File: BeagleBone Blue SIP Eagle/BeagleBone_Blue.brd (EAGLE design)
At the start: 86.4 x 54.6 mm, 281 parts, among them M1 JST_ZH_2, M2 JST_ZH_2, M3 JST_ZH_2, M4 JST_ZH_2, P10 SCHA5B0200, Q3 MOSFET-N, U1 TPD4S012_DRY_6, U4 TPD4S012_DRY_6, U5 24LC_32AT-I/OT, U6 SN74LVC1G07_DCK_5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

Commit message: swap to MicroUSB connector
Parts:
- removed OTG: UX60SC-MB-5ST(80), BeagleBone_Blue:UX60SC-MB-5ST(80)
- added JP1: (no value), Strawson_Eagle_Lib:USB-AB-MICRO-SMD
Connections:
- net GND: now also JP1.GND, JP1.SHIELD1, JP1.SHIELD2, JP1.SHIELD3, JP1.SHIELD4; no longer OTG.5, OTG.M1, OTG.M2, OTG.M3, OTG.M4
- net N$117: now also JP1.D+; no longer OTG.3
- net N$118: now also JP1.D-; no longer OTG.2
- net N$119: now also JP1.ID; no longer OTG.4
- net USB0_VBUS: now also JP1.VBUS; no longer OTG.1

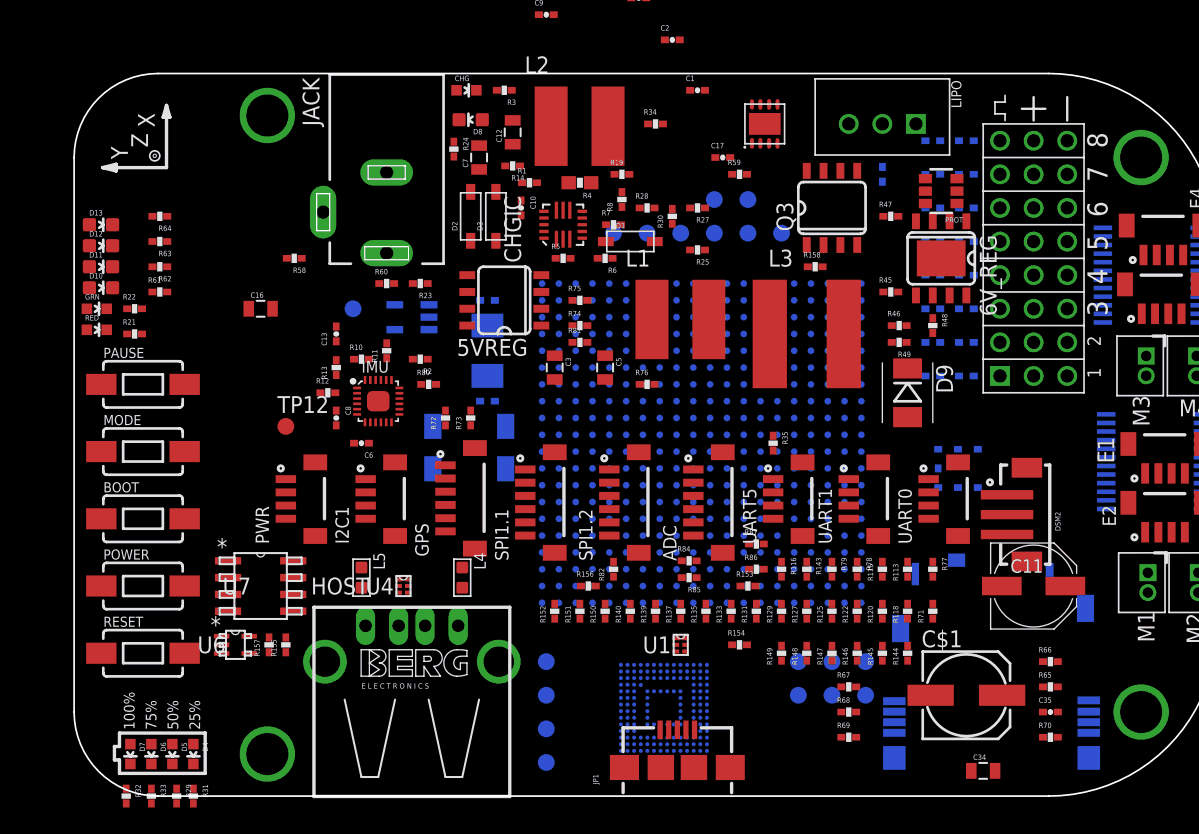
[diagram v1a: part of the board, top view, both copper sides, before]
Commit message: shuffle left side of board and tweak silkscreen for EEPROM
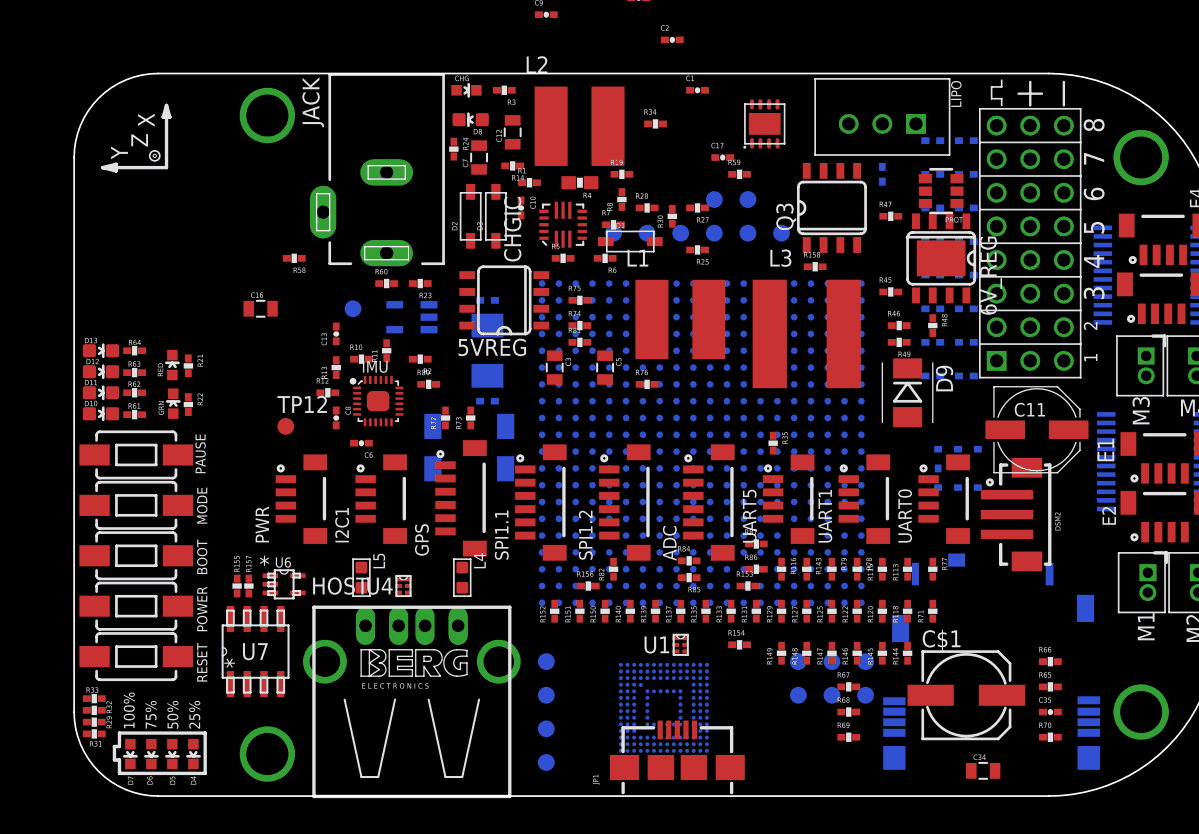
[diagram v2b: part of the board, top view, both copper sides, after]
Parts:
- moved C11 11.8 mm to (72.8, -26.9)
- moved R64 10.3 mm to (4.57, -21.0), turned to 0 degrees
- moved R63 10.1 mm to (4.57, -22.6)
- moved R62 9.71 mm to (4.57, -24.1)
- moved D10 9.53 mm to (2.03, -25.7)
- moved D12 9.53 mm to (2.03, -22.5)
- moved D11 9.52 mm to (2.03, -24.1)
- moved D13 9.52 mm to (2.03, -21.0)
- moved R61 9.46 mm to (4.57, -25.8)
- moved GRN 9.21 mm to (7.49, -25.0), turned to 0 degrees
- moved R31 8.84 mm to (1.52, -49.9), turned to 0 degrees
- moved R33 8.54 mm to (1.52, -47.2), turned to 0 degrees
- moved R29 8.36 mm to (1.52, -49.0), turned to 0 degrees
- moved R22 8.30 mm to (8.64, -25.0), turned to 270 degrees
- moved R32 6.91 mm to (1.52, -48.1), turned to 0 degrees
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
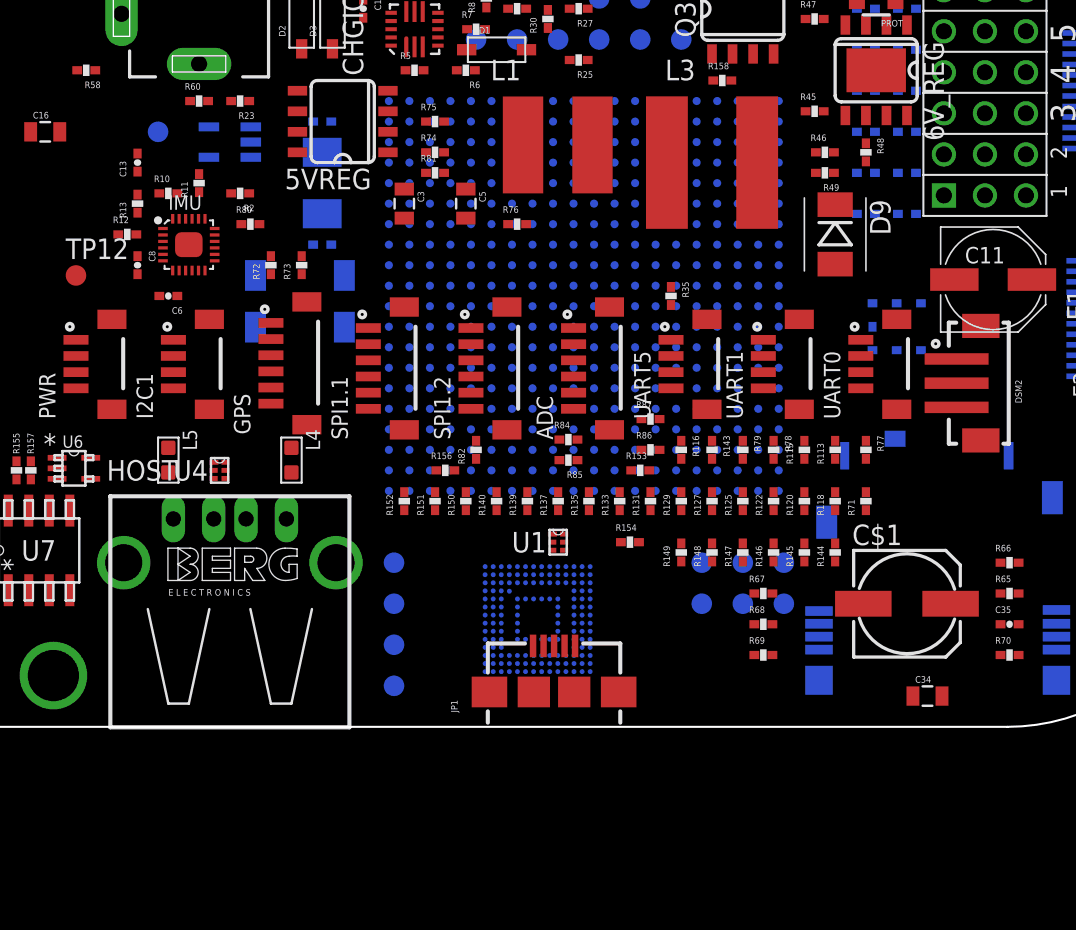
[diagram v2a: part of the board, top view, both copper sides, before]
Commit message: fix incorrect name and origin for usb host port and capacitor in library
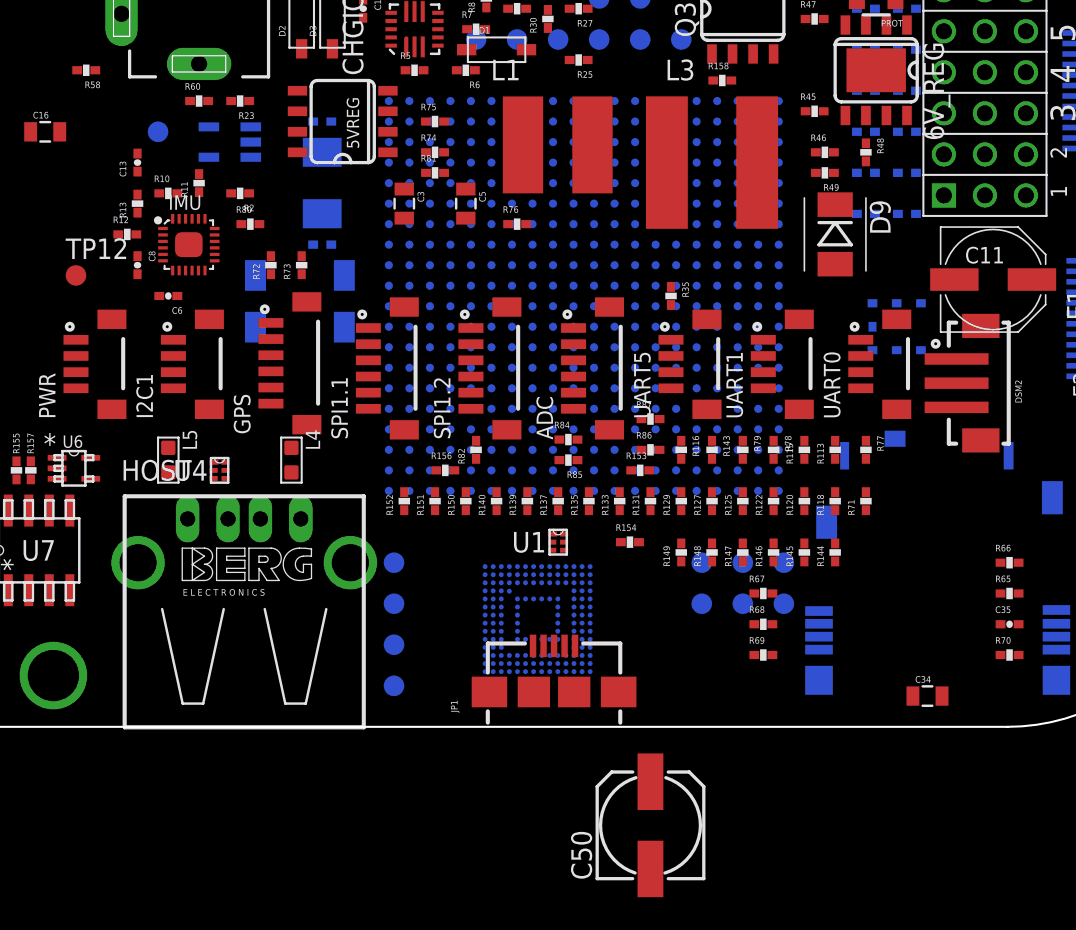
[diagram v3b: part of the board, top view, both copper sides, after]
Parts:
- removed C$1: AVE107M06D16T-F, BeagleBone_Blue:AVE107M06D16T-F
- added C50: AVE107M06D16T-F, BeagleBone_Blue:AVE107M06D16T-F
- moved HOST 10.6 mm to (26.4, -48.0)
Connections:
- net GND: now also C50.-; no longer C$1.-
- net N$127: now also C50.+; no longer C$1.+
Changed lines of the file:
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@@
 <attribute name="VALUE" x="1.699" y="-39.149" size="0.762" layer="27"/>
 </element>
-<element name="C$1" library="BeagleBone_Blue" package="AVE107M06D16T-F" value="AVE107M06D16T-F" x="80.137" y="-49.53"/>
+<element name="C50" library="BeagleBone_Blue" package="AVE107M06D16T-F" value="AVE107M06D16T-F" x="51.562" y="-60.706" rot="R90"/>
 <element name="C1" library="Strawson_Eagle_Lib" package="0402-CAP" value="0.1uF" x="47.117" y="-1.27"/>
 <element name="C10" library="Strawson_Eagle_Lib" package="0402-CAP" value="1uF" x="33.782" y="-10.16" rot="R270"/>
@@
 <element name="H1" library="SparkFun" package="SSOP24" value="TB6621FNG" x="81.407" y="-15.24" rot="MR270"/>
 <element name="H2" library="SparkFun" package="SSOP24" value="TB6621FNG" x="81.661" y="-29.337" rot="MR270"/>
-<element name="HOST" library="BeagleBone_Blue" package="87520-0010BLF" value="87520-0010BLF" x="36.957" y="-46.99"/>
+<element name="HOST" library="BeagleBone_Blue" package="87520-0010BLF" value="87520-0010BLF" x="26.416" y="-48.006"/>
 <element name="I2C1" library="Strawson_Eagle_Lib" package="JST_SH_4_SMD" value="JST_SH_4" x="23.3045" y="-31.115" rot="R90"/>
 <element name="IMU" library="Strawson_Eagle_Lib" package="QFN24G-0.4-3X3MM" value="MPU-9250" x="22.987" y="-24.765">
@@
 <element name="E$1" library="Strawson_Eagle_Lib" package="BATTERY_INDICATOR" value="" x="6.731" y="-51.3715"/>
 <element name="BOARD" library="Strawson_Eagle_Lib" package="BEAGLEBONE_BLUE_NO_HOLES" value="" x="0" y="0" rot="R270"/>
-<element name="5VREG" library="BeagleBone_Blue" package="SO08-TIGHT" value="AP1509SOIC-8-TIGHT" x="32.512" y="-17.145" rot="R90"/>
+<element name="5VREG" library="BeagleBone_Blue" package="SO08-TIGHT" value="AP1509SOIC-8-TIGHT" x="32.512" y="-17.145" smashed="yes" rot="R90">
+<attribute name="VALUE" x="33.147" y="-18.669" size="1.27" layer="27" ratio="10" rot="R90"/>
+<attribute name="NAME" x="32.766" y="-15.621" size="0.762" layer="25" ratio="10" rot="R270"/>
+</element>
 <element name="JP1" library="Strawson_Eagle_Lib" package="USB-AB-MICRO-SMD" value="" x="45.593" y="-52.451" rot="R90"/>
 </elements>
@@
 <contactref element="U4" pad="4"/>
 <contactref element="L4" pad="1"/>
-<contactref element="C$1" pad="-"/>
+<contactref element="C50" pad="-"/>
 <contactref element="C45" pad="2"/>
 <contactref element="C46" pad="2"/>
@@
 <wire x1="62.468" y1="-41.948" x2="62.992" y2="-38.0238" width="0" layer="19" extent="1-16"/>
 <wire x1="58.547" y1="-30.655" x2="53.1495" y2="-29.845" width="0" layer="19" extent="1-16"/>
-<wire x1="64.737" y1="-46.99" x2="62.468" y2="-41.948" width="0" layer="19" extent="1-16"/>
-<wire x1="61.992" y1="-51.73" x2="64.737" y2="-46.99" width="0" layer="19" extent="1-16"/>
+<wire x1="51.562" y1="-63.406" x2="62.468" y2="-41.948" width="0" layer="19" extent="1-16"/>
+<wire x1="61.992" y1="-51.73" x2="51.562" y2="-63.406" width="0" layer="19" extent="1-16"/>
 <wire x1="18.822" y1="-10.4775" x2="23.622" y2="-7.4775" width="0" layer="19" extent="1-1"/>
 <wire x1="67.807" y1="-52.705" x2="61.992" y2="-51.73" width="0" layer="19" extent="1-16"/>
@@
 <wire x1="29.337" y1="-37.338" x2="28.067" y2="-34.6075" width="0" layer="19" extent="1-1"/>
 <wire x1="25.262003125" y1="-39.235" x2="29.337" y2="-37.338" width="0" layer="19" extent="1-1"/>
-<wire x1="32.097" y1="-44.45" x2="35.3695" y2="-38.735" width="0" layer="19" extent="16-16"/>
+<wire x1="32.986" y1="-44.45" x2="35.3695" y2="-38.735" width="0" layer="19" extent="16-16"/>
 <wire x1="73.2282" y1="-48.26" x2="67.807" y2="-52.705" width="0" layer="19" extent="1-1"/>
 <wire x1="76.692" y1="-49.03" x2="73.2282" y2="-48.26" width="0" layer="19" extent="1-16"/>
@@
 <wire x1="85.063" y1="-16.865" x2="85.063" y2="-13.615" width="0" layer="19" extent="16-16"/>
 <wire x1="85.063" y1="-17.515" x2="85.063" y2="-16.865" width="0" layer="19" extent="16-16"/>
-<wire x1="18.957" y1="-44.45" x2="14.8336" y2="-39.2579875" width="0" layer="19" extent="1-1"/>
+<wire x1="19.846" y1="-44.45" x2="14.8336" y2="-39.2579875" width="0" layer="19" extent="1-1"/>
 <wire x1="1.549" y1="-32.639" x2="7.849" y2="-36.449" width="0" layer="19" extent="1-1"/>
 <wire x1="1.549" y1="-28.829" x2="1.549" y2="-32.639" width="0" layer="19" extent="1-1"/>
@@
 <contactref element="HOST" pad="3"/>
 <contactref element="U4" pad="1"/>
-<wire x1="24.536984375" y1="-38.235" x2="26.527" y2="-41.74" width="0" layer="19" extent="1-1"/>
-<wire x1="39.1795" y1="-33.655" x2="26.527" y2="-41.74" width="0" layer="19" extent="16-16"/>
+<wire x1="24.536984375" y1="-38.235" x2="27.416" y2="-41.74" width="0" layer="19" extent="1-1"/>
+<wire x1="39.1795" y1="-33.655" x2="27.416" y2="-41.74" width="0" layer="19" extent="16-16"/>
 </signal>
 <signal name="N$124">
@@
 <contactref element="HOST" pad="2"/>
 <contactref element="U4" pad="2"/>
-<wire x1="24.521996875" y1="-38.735" x2="24.527" y2="-41.74" width="0" layer="19" extent="1-1"/>
+<wire x1="24.521996875" y1="-38.735" x2="25.416" y2="-41.74" width="0" layer="19" extent="1-1"/>
 <wire x1="37.9095" y1="-33.655" x2="24.521996875" y2="-38.735" width="0" layer="19" extent="1-16"/>
 </signal>
@@
 <contactref element="U7" pad="2"/>
 <contactref element="U7" pad="3"/>
-<contactref element="C$1" pad="+"/>
+<contactref element="C50" pad="+"/>
 <wire x1="14.351" y1="-46.1518" x2="13.081" y2="-46.1518" width="0" layer="19" extent="1-1"/>
 <wire x1="36.322" y1="-40.0812" x2="14.351" y2="-46.1518" width="0" layer="19" extent="1-1"/>
 <wire x1="51.4858" y1="-38.735" x2="36.322" y2="-40.0812" width="0" layer="19" extent="1-1"/>
-<wire x1="70.137" y1="-46.99" x2="51.4858" y2="-38.735" width="0" layer="19" extent="1-1"/>
+<wire x1="51.562" y1="-58.006" x2="51.4858" y2="-38.735" width="0" layer="19" extent="1-1"/>
 </signal>
 <signal name="USB0_VBUS">
@@
 <contactref element="L4" pad="2"/>
 <contactref element="HOST" pad="4"/>
-<wire x1="29.337" y1="-38.862" x2="29.027" y2="-41.74" width="0" layer="19" extent="1-1"/>
+<wire x1="29.337" y1="-38.862" x2="29.916" y2="-41.74" width="0" layer="19" extent="1-1"/>
 </signal>
 <signal name="N$129">
@@
 <contactref element="L5" pad="2"/>
 <contactref element="HOST" pad="1"/>
-<wire x1="21.717" y1="-38.862" x2="22.027" y2="-41.74" width="0" layer="19" extent="1-1"/>
+<wire x1="21.717" y1="-38.862" x2="22.916" y2="-41.74" width="0" layer="19" extent="1-1"/>
 </signal>
 <signal name="N$131">
